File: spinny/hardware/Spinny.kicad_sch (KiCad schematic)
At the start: 36 parts, among them J1 USB_C_Receptacle_USB2.0, J2 Conn_01x04, SW1 SW_Push, SW2 SW_Push, SW3 SW_Push, SW4 SW_Push, SW5 SW_RST, U1 XC6206P332MR, U2 SRV05-4, U3 STM32F103C8T6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

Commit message: Update part numbers and automate Gerber, BOM and CPL files
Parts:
- C1, C12, C2, C8: LCSC (none) -> C52923
- C10, C11: LCSC (none) -> C1570
- C3: LCSC (none) -> C19666
- C4, C5, C6, C7: LCSC (none) -> C1525
- C9: LCSC (none) -> C15195
- D1: JLCPCB Part # C72043 -> (none); LCSC (none) -> C72043
- D2: JLCPCB Part # C2290 -> (none); LCSC (none) -> C2290
- J1: JLCPCB Part # C709357 -> (none); LCSC (none) -> C709357
- R1, R2: LCSC (none) -> C25905
- R3: LCSC (none) -> C25091
- R4: LCSC (none) -> C25741
- R5: LCSC (none) -> C25867
- R6: LCSC (none) -> C25104
- SW5: LCSC (none) -> C318884
- U1: LCSC (none) -> C5446
- U2: JLCPCB Part # C85364 -> (none); LCSC (none) -> C85364
- U3: JLCPCB Part # C8734 -> (none); LCSC (none) -> C8734
- Y1: JLCPCB Part # C115962 -> (none); LCSC (none) -> C115962

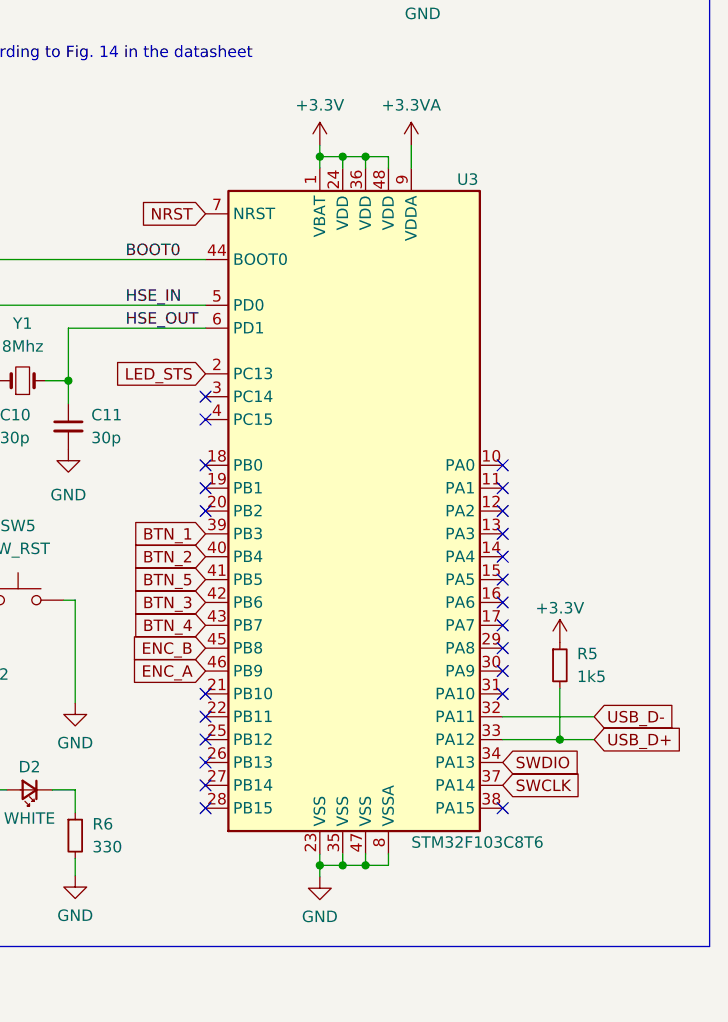
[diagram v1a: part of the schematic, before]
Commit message: Spinny V2 with stm32f104cbt6 instead of c8t6, because JLCPCB is random
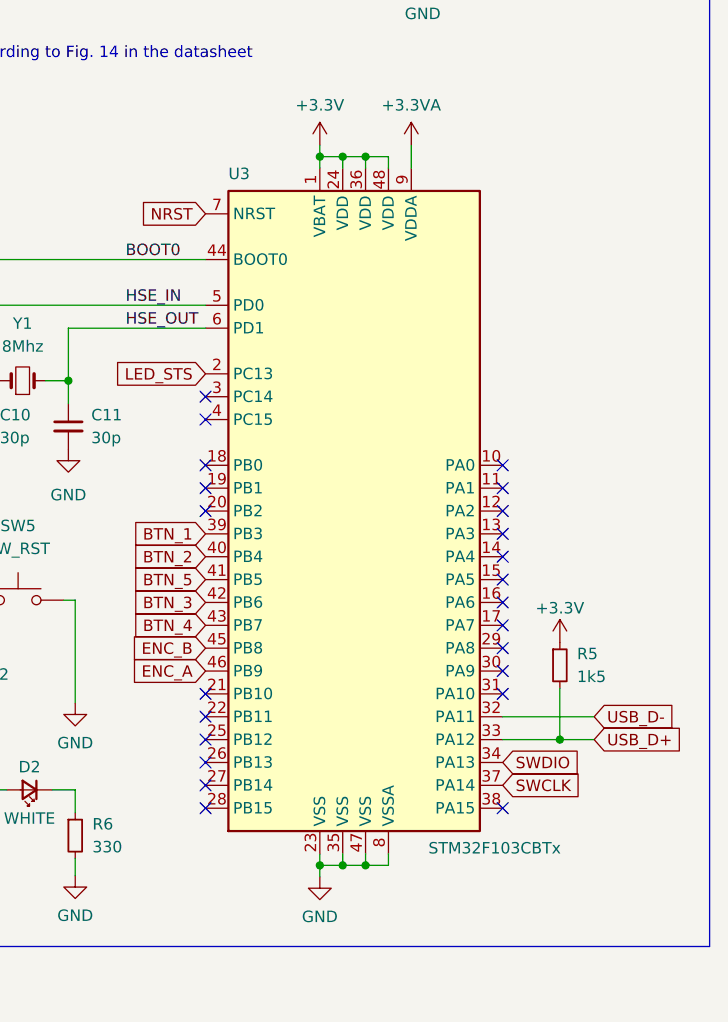
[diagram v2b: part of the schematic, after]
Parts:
- removed U3: STM32F103C8T6, Package_QFP:LQFP-48_7x7mm_P0.5mm, symbol MCU_ST_STM32F1:STM32F103C8Tx
- added U3: STM32F103CBTx, Package_QFP:LQFP-48_7x7mm_P0.5mm, symbol MCU_ST_STM32F1:STM32F103CBTx
- MT1: footprint DigiKey:XDCR_PEC11R-4215F-S0024 -> XDCR_PEC11R-4215F-S0024
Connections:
- net BOOT0: now also U3.44 (BOOT0)
- net BTN_1: now also U3.39 (PB3)
- net BTN_2: now also U3.40 (PB4)
- net BTN_3: now also U3.42 (PB6)
- net BTN_4: now also U3.43 (PB7)
- net BTN_5: now also U3.41 (PB5)
- net ENC_A: now also U3.46 (PB9)
- net ENC_B: now also U3.45 (PB8)
- net GND: now also U3.23 (VSS), U3.35 (VSS), U3.47 (VSS), U3.8 (VSSA)
- net HSE_IN: now also U3.5 (PD0)
- net HSE_OUT: now also U3.6 (PD1)
- net LED_STS: now also U3.2 (PC13)
- net NRST: now also U3.7 (NRST)
- net SWCLK: now also U3.37 (PA14)
- net SWDIO: now also U3.34 (PA13)
- net USB_D+: now also U3.33 (PA12)
- net USB_D-: now also U3.32 (PA11)
- net +3.3VA renamed +3.3V
- net +3.3V: now also U3.1 (VBAT), U3.24 (VDD), U3.36 (VDD), U3.48 (VDD), U3.9 (VDDA)
